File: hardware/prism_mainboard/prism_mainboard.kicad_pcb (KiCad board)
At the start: 2 copper layers, 11 parts, among them U1 XC7Z010-1CLG400C

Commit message: Origin Update
origin update
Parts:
- added C10: 10uF, Capacitor_SMD:C_0805_2012Metric, F.Cu at (251.5, 116.3)
- added C11: 4.7uF, Capacitor_SMD:C_0805_2012Metric, F.Cu at (251.5, 119.3)
- added C12: 2.2uF, Capacitor_SMD:C_0201_0603Metric, F.Cu at (259.5, 122.4)
- added C13: 10uF, Capacitor_SMD:C_0805_2012Metric, F.Cu at (251.5, 122.3)
- added C14: 1uF, Capacitor_SMD:C_0201_0603Metric, F.Cu at (259.5, 124.2)
- added C15: 2.2uF, Capacitor_SMD:C_0201_0603Metric, F.Cu at (259.5, 125.9)
- added C8: 22uF, Capacitor_SMD:C_1206_3216Metric, F.Cu at (256.5, 116.5)
- added C9: 22uF, Capacitor_SMD:C_1206_3216Metric, F.Cu at (256.5, 119.8)
- added L1: 0.47uH, Inductor_SMD:L_0805_2012Metric, F.Cu at (256.0, 122.9)
- added L2: 0.47uH, Inductor_SMD:L_0805_2012Metric, F.Cu at (256.0, 125.7)

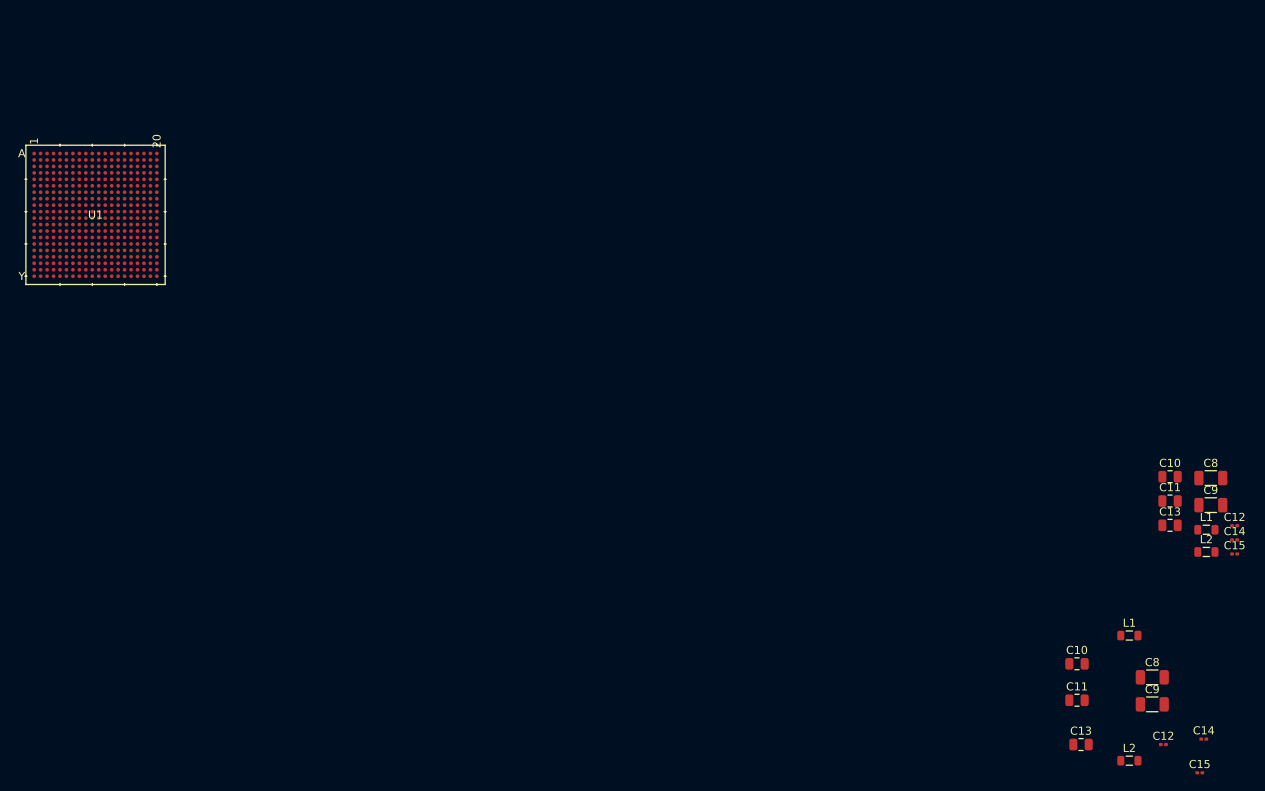
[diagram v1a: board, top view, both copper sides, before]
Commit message: Mainboard Updates
Started a lot of the basic schematic nets like GND and Power nets. Major Change: Decided on using the XC7Z015-1CLG485I instead of the 7010 or 7020 due to the ability to use HDMI interfaces with an adapter and more LUTs. Updated schematic symbols and footprints accordingly. Added Memory, Encoder, MicroSD schematics. Added LimeSDR footprints as well. Will Try to add Power to the entire board next.
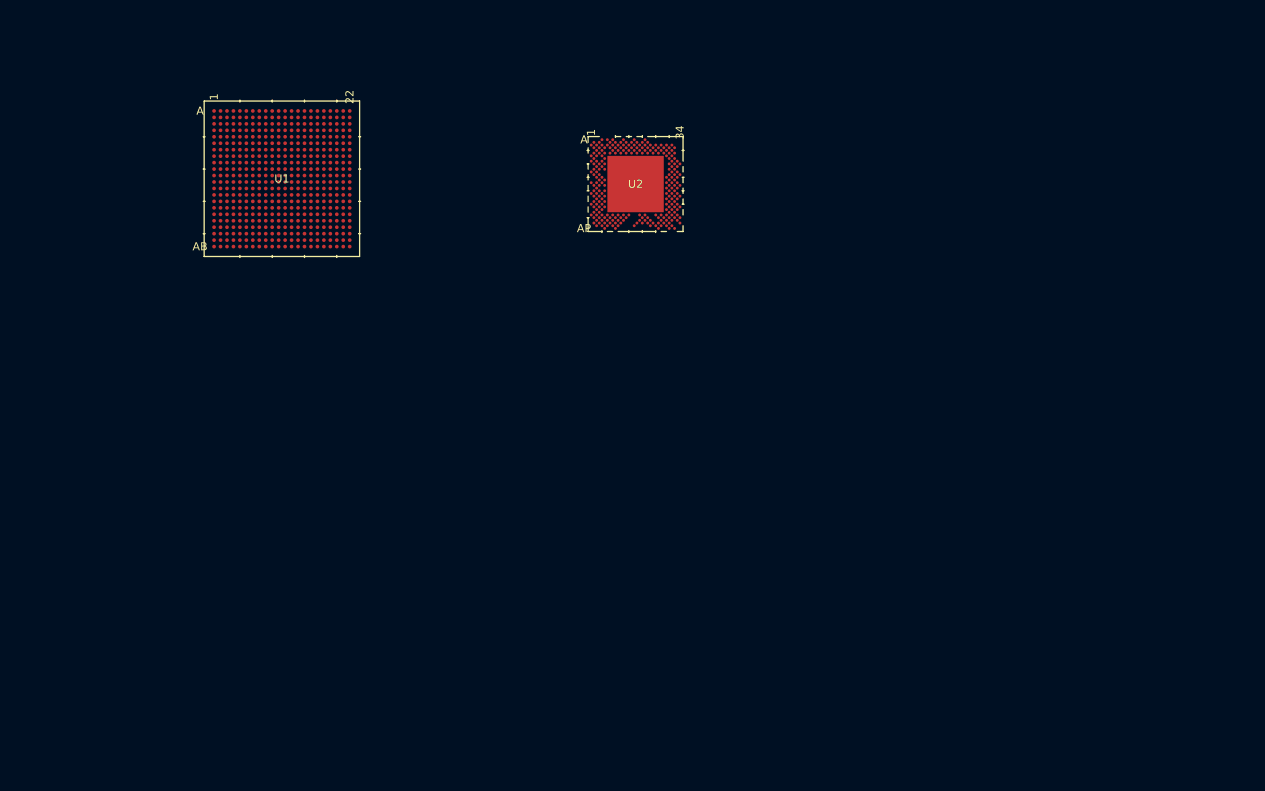
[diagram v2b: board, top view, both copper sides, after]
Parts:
- removed C10 (x2), C13 (x2): 10uF, Capacitor_SMD:C_0805_2012Metric
- removed C11 (x2): 4.7uF, Capacitor_SMD:C_0805_2012Metric
- removed C12 (x2), C15 (x2): 2.2uF, Capacitor_SMD:C_0201_0603Metric
- removed C14 (x2): 1uF, Capacitor_SMD:C_0201_0603Metric
- removed C8 (x2), C9 (x2): 22uF, Capacitor_SMD:C_1206_3216Metric
- removed L1 (x2), L2 (x2): 0.47uH, Inductor_SMD:L_0805_2012Metric
- added U2: LMS7002M, LMS7002M:AQFN261_11P5X11P5_LIM, F.Cu at (185.3, 80.1)
- U1: value XC7Z010-1CLG400C -> XC7Z015-2CLG485I; footprint XC7Z010-1CLG400C:CLG400_XIL -> footprints:CLG485_XIL
- moved U1 23.5 mm to (141.5, 79.4)
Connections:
- U1 pad A10: (no net) -> unconnected-(U1B-PS_MIO26_501-PadA10)
- U1 pad A11: (no net) -> unconnected-(U1B-PS_MIO28_501-PadA11)
- U1 pad A12: (no net) -> unconnected-(U1B-PS_MIO30_501-PadA12)
- U1 pad A13: (no net) -> unconnected-(U1B-VCCO_MIO1_501-PadA13)
- U1 pad A14: (no net) -> unconnected-(U1B-PS_MIO36_501-PadA14)
- U1 pad A15: (no net) -> unconnected-(U1B-PS_MIO20_501-PadA15)
- U1 pad A16: (no net) -> unconnected-(U1B-PS_MIO18_501-PadA16)
- U1 pad A17: (no net) -> unconnected-(U1B-PS_MIO13_500-PadA17)
- U1 pad A18: (no net) -> GND
- U1 pad A19: (no net) -> unconnected-(U1B-PS_MIO6_500-PadA19)
- U1 pad A20: (no net) -> unconnected-(U1B-PS_MIO5_500-PadA20)
- U1 pad A8: unconnected-(U1A-GND-PadA8) -> GND
- U1 pad B10: (no net) -> unconnected-(U1C-VCCO_MIO1_501-PadB10)
- U1 pad B11: (no net) -> unconnected-(U1C-PS_MIO34_501-PadB11)
- U1 pad B12: (no net) -> unconnected-(U1C-PS_MIO43_501-PadB12)
- U1 pad B13: (no net) -> unconnected-(U1C-PS_MIO47_501-PadB13)
- U1 pad B14: (no net) -> unconnected-(U1C-PS_MIO45_501-PadB14)
- U1 pad B15: (no net) -> GND
- U1 pad B16: (no net) -> unconnected-(U1C-PS_MIO24_501-PadB16)
- U1 pad B17: (no net) -> unconnected-(U1C-PS_MIO14_500-PadB17)
- U1 pad B18: (no net) -> unconnected-(U1C-PS_POR_B_500-PadB18)
- U1 pad B19: (no net) -> unconnected-(U1C-PS_MIO11_500-PadB19)
- U1 pad B20: (no net) -> unconnected-(U1C-VCCO_MIO0_500-PadB20)
- U1 pad B5: unconnected-(U1A-PS_MIO9_500-PadB5) -> GND
- U1 pad C10: (no net) -> unconnected-(U1C-PS_MIO39_501-PadC10)
- U1 pad C11: (no net) -> unconnected-(U1C-PS_MIO53_501-PadC11)
- U1 pad C12: (no net) -> GND
- U1 pad C13: (no net) -> unconnected-(U1C-PS_MIO51_501-PadC13)
- U1 pad C14: (no net) -> unconnected-(U1C-PS_SRST_B_501-PadC14)
- U1 pad C15: (no net) -> unconnected-(U1C-PS_MIO41_501-PadC15)
- U1 pad C16: (no net) -> unconnected-(U1C-PS_MIO32_501-PadC16)
- U1 pad C17: (no net) -> unconnected-(U1C-VCCO_MIO0_500-PadC17)
- U1 pad C18: (no net) -> unconnected-(U1C-PS_MIO12_500-PadC18)
- U1 pad C19: (no net) -> unconnected-(U1C-PS_MIO9_500-PadC19)
- U1 pad C2: unconnected-(U1A-PS_DDR_DQS_P0_502-PadC2) -> GND
- U1 pad C20: (no net) -> unconnected-(U1C-PS_DDR_DQ1_502-PadC20)
- U1 pad D10: (no net) -> unconnected-(U1C-PS_MIO50_501-PadD10)
- U1 pad D11: (no net) -> unconnected-(U1C-PS_MIO46_501-PadD11)
- U1 pad D12: (no net) -> unconnected-(U1C-PS_MIO48_501-PadD12)
- U1 pad D13: (no net) -> unconnected-(U1C-PS_MIO52_501-PadD13)
- U1 pad D14: (no net) -> unconnected-(U1C-VCCO_MIO1_501-PadD14)
- U1 pad D15: (no net) -> unconnected-(U1C-PS_MIO42_501-PadD15)
- U1 pad D16: (no net) -> unconnected-(U1C-PS_MIO27_501-PadD16)
- U1 pad D17: (no net) -> unconnected-(U1C-PS_MIO16_501-PadD17)
- U1 pad D18: (no net) -> unconnected-(U1C-PS_MIO7_500-PadD18)
- U1 pad D19: (no net) -> GND
- U1 pad D20: (no net) -> unconnected-(U1C-PS_DDR_DQ3_502-PadD20)
- U1 pad D9: unconnected-(U1A-PS_MIO12_500-PadD9) -> GND
- U1 pad E10: (no net) -> unconnected-(U1C-PS_MIO44_501-PadE10)
- U1 pad E11: (no net) -> unconnected-(U1C-VCCO_MIO1_501-PadE11)
- U1 pad E12: (no net) -> unconnected-(U1C-PS_MIO23_501-PadE12)
- U1 pad E13: (no net) -> unconnected-(U1C-PS_MIO19_501-PadE13)
- U1 pad E14: (no net) -> unconnected-(U1C-PS_MIO17_501-PadE14)
- U1 pad E15: (no net) -> unconnected-(U1C-PS_MIO29_501-PadE15)
- U1 pad E16: (no net) -> GND
- U1 pad E17: (no net) -> unconnected-(U1C-PS_MIO15_500-PadE17)
- U1 pad E18: (no net) -> unconnected-(U1C-PS_MIO8_500-PadE18)
- U1 pad E19: (no net) -> unconnected-(U1C-PS_MIO4_500-PadE19)
- U1 pad E20: (no net) -> unconnected-(U1C-PS_DDR_DQ4_502-PadE20)
- U1 pad E6: unconnected-(U1A-PS_MIO0_500-PadE6) -> GND
- U1 pad F10: (no net) -> unconnected-(U1C-PS_MIO38_501-PadF10)
- U1 pad F11: (no net) -> unconnected-(U1C-PS_MIO25_501-PadF11)
- U1 pad F12: (no net) -> unconnected-(U1C-PS_MIO21_501-PadF12)
- U1 pad F13: (no net) -> GND
- U1 pad F14: (no net) -> unconnected-(U1C-PS_MIO31_501-PadF14)
- U1 pad F15: (no net) -> unconnected-(U1C-PS_MIO_VREF_501-PadF15)
- U1 pad F16: (no net) -> unconnected-(U1C-PS_CLK_500-PadF16)
- U1 pad F17: (no net) -> unconnected-(U1C-PS_MIO3_500-PadF17)
- U1 pad F18: (no net) -> unconnected-(U1C-VCCO_DDR_502-PadF18)
- U1 pad F19: (no net) -> unconnected-(U1C-PS_DDR_A13_502-PadF19)
- U1 pad F20: (no net) -> unconnected-(U1C-PS_DDR_DRST_B_502-PadF20)
- U1 pad F3: unconnected-(U1A-GND-PadF3) -> GND
- U1 pad G10: (no net) -> GND
- U1 pad G11: (no net) -> unconnected-(U1C-PS_MIO33_501-PadG11)
- U1 pad G12: (no net) -> unconnected-(U1C-RSVDGND-PadG12)
- U1 pad G13: (no net) -> VCCPINT
- U1 pad G14: (no net) -> unconnected-(U1C-VCCBATT_0-PadG14)
- U1 pad G15: (no net) -> VCCPINT
- U1 pad G16: (no net) -> unconnected-(U1C-PS_MIO10_500-PadG16)
- U1 pad G17: (no net) -> unconnected-(U1C-PS_MIO0_500-PadG17)
- U1 pad G18: (no net) -> unconnected-(U1C-PS_DDR_A11_502-PadG18)
- U1 pad G19: (no net) -> unconnected-(U1C-PS_DDR_A14_502-PadG19)
- U1 pad G20: (no net) -> GND
- U1 pad H10: (no net) -> unconnected-(U1C-TMS_0-PadH10)
- U1 pad H11: (no net) -> unconnected-(U1C-TCK_0-PadH11)
- U1 pad H12: (no net) -> unconnected-(U1D-VCCBRAM-PadH12)
- U1 pad H13: (no net) -> GND
- U1 pad H14: (no net) -> VCCPINT
- U1 pad H15: (no net) -> GND
- U1 pad H16: (no net) -> unconnected-(U1D-PS_DDR_VREF0_502-PadH16)
- U1 pad H17: (no net) -> GND
- U1 pad H18: (no net) -> unconnected-(U1D-PS_DDR_A9_502-PadH18)
- U1 pad H19: (no net) -> unconnected-(U1D-PS_DDR_A12_502-PadH19)
- U1 pad H20: (no net) -> unconnected-(U1D-PS_DDR_DM1_502-PadH20)
- U1 pad H7: unconnected-(U1A-GND-PadH7) -> GND
- U1 pad J10: (no net) -> GND
- U1 pad J11: (no net) -> VCCINT
- U1 pad J12: (no net) -> GND
- U1 pad J13: (no net) -> unconnected-(U1D-VCCBRAM-PadJ13)
- U1 pad J14: (no net) -> GND
- U1 pad J15: (no net) -> VCCPINT
- U1 pad J16: (no net) -> unconnected-(U1D-PS_DDR_A6_502-PadJ16)
- U1 pad J17: (no net) -> unconnected-(U1D-PS_DDR_A7_502-PadJ17)
- U1 pad J18: (no net) -> unconnected-(U1D-PS_DDR_A8_502-PadJ18)
- U1 pad J19: (no net) -> unconnected-(U1D-VCCO_DDR_502-PadJ19)
- U1 pad J20: (no net) -> unconnected-(U1D-PS_DDR_A10_502-PadJ20)
- U1 pad J4: unconnected-(U1A-PS_DDR_A9_502-PadJ4) -> GND
- U1 pad J9: unconnected-(U1A-VCCADC_0-PadJ9) -> VCCINT
- U1 pad K1: unconnected-(U1A-PS_DDR_A8_502-PadK1) -> GND
- U1 pad K10: (no net) -> VCCINT
- U1 pad K11: (no net) -> unconnected-(U1D-GNDADC_0-PadK11)
- U1 pad K12: (no net) -> unconnected-(U1D-VCCADC_0-PadK12)
- U1 pad K13: (no net) -> GND
- U1 pad K14: (no net) -> unconnected-(U1D-VCCPAUX-PadK14)
- U1 pad K15: (no net) -> GND
- U1 pad K16: (no net) -> unconnected-(U1D-VCCO_DDR_502-PadK16)
- U1 pad K17: (no net) -> unconnected-(U1D-PS_DDR_A4_502-PadK17)
- U1 pad K18: (no net) -> unconnected-(U1D-PS_DDR_A5_502-PadK18)
- U1 pad K19: (no net) -> unconnected-(U1D-PS_DDR_A2_502-PadK19)
- U1 pad K20: (no net) -> unconnected-(U1D-PS_DDR_DQ15_502-PadK20)
- U1 pad K9: unconnected-(U1A-VP_0-PadK9) -> GND
- U1 pad L10: (no net) -> GND
- U1 pad L11: (no net) -> unconnected-(U1D-VREFN_0-PadL11)
- U1 pad L12: (no net) -> unconnected-(U1D-VP_0-PadL12)
- U1 pad L13: (no net) -> unconnected-(U1D-VCCPAUX-PadL13)
- U1 pad L14: (no net) -> GND
- U1 pad L15: (no net) -> VCCPINT
- U1 pad L16: (no net) -> unconnected-(U1D-PS_DDR_BA0_502-PadL16)
- U1 pad L17: (no net) -> unconnected-(U1D-PS_DDR_BA1_502-PadL17)
- U1 pad L18: (no net) -> GND
- U1 pad L19: (no net) -> unconnected-(U1D-PS_DDR_A3_502-PadL19)
- U1 pad L20: (no net) -> unconnected-(U1D-PS_DDR_DQ12_502-PadL20)
- U1 pad L8: unconnected-(U1A-GND-PadL8) -> GND
- U1 pad L9: unconnected-(U1A-VREFP_0-PadL9) -> VCCINT
- U1 pad M10: (no net) -> VCCINT
- U1 pad M11: (no net) -> unconnected-(U1D-VN_0-PadM11)
- U1 pad M12: (no net) -> unconnected-(U1D-VREFP_0-PadM12)
- U1 pad M13: (no net) -> GND
- U1 pad M14: (no net) -> unconnected-(U1D-VCCPAUX-PadM14)
- U1 pad M15: (no net) -> GND
- U1 pad M16: (no net) -> unconnected-(U1D-PS_DDR_VRN_502-PadM16)
- U1 pad M17: (no net) -> unconnected-(U1D-PS_DDR_BA2_502-PadM17)
- U1 pad M18: (no net) -> unconnected-(U1D-PS_DDR_A1_502-PadM18)
- U1 pad M19: (no net) -> unconnected-(U1D-PS_DDR_A0_502-PadM19)
- U1 pad M2: (no net) -> unconnected-(U1B-IO_L15P_T2_DQS_34-PadM2)
- U1 pad M20: (no net) -> unconnected-(U1D-VCCO_DDR_502-PadM20)
- U1 pad M3: (no net) -> unconnected-(U1B-IO_L22N_T3_34-PadM3)
- U1 pad M4: (no net) -> unconnected-(U1B-IO_L22P_T3_34-PadM4)
- U1 pad M5: (no net) -> GND
- U1 pad M6: (no net) -> unconnected-(U1B-IO_L4N_T0_34-PadM6)
- U1 pad M7: (no net) -> unconnected-(U1B-IO_L6N_T0_VREF_34-PadM7)
- U1 pad M8: (no net) -> unconnected-(U1B-IO_L6P_T0_34-PadM8)
- U1 pad M9: (no net) -> GND
- U1 pad N1: (no net) -> unconnected-(U1B-IO_L16P_T2_34-PadN1)
- U1 pad N10: (no net) -> GND
- U1 pad N11: (no net) -> unconnected-(U1D-DXN_0-PadN11)
- U1 pad N12: (no net) -> unconnected-(U1D-DXP_0-PadN12)
- U1 pad N13: (no net) -> VCCAUX
- U1 pad N14: (no net) -> GND
- U1 pad N15: (no net) -> VCCPINT
- U1 pad N16: (no net) -> unconnected-(U1D-PS_DDR_VRP_502-PadN16)
- U1 pad N17: (no net) -> unconnected-(U1D-VCCO_DDR_502-PadN17)
- U1 pad N18: (no net) -> unconnected-(U1D-PS_DDR_CKN_502-PadN18)
- U1 pad N19: (no net) -> unconnected-(U1D-PS_DDR_CKP_502-PadN19)
- U1 pad N2: (no net) -> GND
- U1 pad N20: (no net) -> unconnected-(U1D-PS_DDR_DQ18_502-PadN20)
- U1 pad N3: (no net) -> unconnected-(U1B-IO_L21N_T3_DQS_34-PadN3)
- U1 pad N4: (no net) -> unconnected-(U1B-IO_L21P_T3_DQS_34-PadN4)
- U1 pad N5: (no net) -> unconnected-(U1B-IO_L19N_T3_VREF_34-PadN5)
- U1 pad N6: (no net) -> unconnected-(U1B-IO_L19P_T3_34-PadN6)
- U1 pad N7: (no net) -> unconnected-(U1B-VCCO_34-PadN7)
- U1 pad N8: (no net) -> unconnected-(U1B-IO_L5P_T0_34-PadN8)
- U1 pad N9: (no net) -> VCCINT
- U1 pad P1: (no net) -> unconnected-(U1B-IO_L16N_T2_34-PadP1)
- U1 pad P10: (no net) -> VCCINT
- U1 pad P11: (no net) -> GND
- U1 pad P12: (no net) -> VCCAUX
- U1 pad P13: (no net) -> GND
- U1 pad P14: (no net) -> unconnected-(U1D-VCCPAUX-PadP14)
- U1 pad P15: (no net) -> GND
- U1 pad P16: (no net) -> unconnected-(U1D-PS_DDR_VREF1_502-PadP16)
- U1 pad P17: (no net) -> unconnected-(U1D-PS_DDR_CS_B_502-PadP17)
- U1 pad P18: (no net) -> unconnected-(U1D-PS_DDR_ODT_502-PadP18)
- U1 pad P19: (no net) -> GND
- U1 pad P2: (no net) -> unconnected-(U1B-IO_L18N_T2_34-PadP2)
- U1 pad P20: (no net) -> unconnected-(U1D-PS_DDR_CAS_B_502-PadP20)
- U1 pad P3: (no net) -> unconnected-(U1B-IO_L18P_T2_34-PadP3)
- U1 pad P4: (no net) -> unconnected-(U1B-VCCO_34-PadP4)
- U1 pad P5: (no net) -> unconnected-(U1B-IO_L20N_T3_34-PadP5)
- U1 pad P6: (no net) -> unconnected-(U1B-IO_L20P_T3_34-PadP6)
- U1 pad P7: (no net) -> unconnected-(U1B-IO_L24P_T3_34-PadP7)
- U1 pad P8: (no net) -> unconnected-(U1B-IO_L5N_T0_34-PadP8)
- U1 pad P9: (no net) -> GND
- U1 pad R1: (no net) -> unconnected-(U1B-VCCO_34-PadR1)
- U1 pad R10: (no net) -> unconnected-(U1D-GND-PadR10)
- U1 pad R11: (no net) -> unconnected-(U1D-VCCO_0-PadR11)
- U1 pad R12: (no net) -> GND
- U1 pad R13: (no net) -> VCCAUX
- U1 pad R14: (no net) -> GND
- U1 pad R15: (no net) -> VCCPINT
- U1 pad R16: (no net) -> GND
- U1 pad R17: (no net) -> unconnected-(U1D-IO_L19P_T3_13-PadR17)
- U1 pad R18: (no net) -> unconnected-(U1E-PS_DDR_RAS_B_502-PadR18)
- U1 pad R19: (no net) -> unconnected-(U1E-PS_DDR_WE_B_502-PadR19)
- U1 pad R2: (no net) -> unconnected-(U1B-IO_L17N_T2_34-PadR2)
- U1 pad R20: (no net) -> unconnected-(U1E-PS_DDR_DQ20_502-PadR20)
- U1 pad R3: (no net) -> unconnected-(U1B-IO_L17P_T2_34-PadR3)
- U1 pad R4: (no net) -> unconnected-(U1B-IO_L23N_T3_34-PadR4)
- U1 pad R5: (no net) -> unconnected-(U1B-IO_L23P_T3_34-PadR5)
- U1 pad R6: (no net) -> GND
- U1 pad R7: (no net) -> unconnected-(U1B-IO_L24N_T3_34-PadR7)
- U1 pad R8: (no net) -> unconnected-(U1B-IO_25_34-PadR8)
- U1 pad R9: (no net) -> VCCINT
- U1 pad T1: (no net) -> unconnected-(U1B-IO_L13N_T2_MRCC_34-PadT1)
- U1 pad T10: (no net) -> unconnected-(U1E-DONE_0-PadT10)
- U1 pad T11: (no net) -> unconnected-(U1E-RSVDVCC3-PadT11)
- U1 pad T12: (no net) -> VCCAUX
- U1 pad T13: (no net) -> GND
- U1 pad T14: (no net) -> unconnected-(U1E-RSVDVCC2-PadT14)
- U1 pad T15: (no net) -> unconnected-(U1E-RSVDVCC1-PadT15)
- U1 pad T16: (no net) -> unconnected-(U1E-IO_0_13-PadT16)
- U1 pad T17: (no net) -> unconnected-(U1E-IO_L19N_T3_VREF_13-PadT17)
- U1 pad T18: (no net) -> unconnected-(U1E-VCCO_13-PadT18)
- U1 pad T19: (no net) -> unconnected-(U1E-PS_DDR_CKE_502-PadT19)
- U1 pad T2: (no net) -> unconnected-(U1B-IO_L13P_T2_MRCC_34-PadT2)
- U1 pad T20: (no net) -> unconnected-(U1E-PS_DDR_DQ17_502-PadT20)
- U1 pad T3: (no net) -> GND
- U1 pad T4: (no net) -> GND
- U1 pad T5: (no net) -> GND
- U1 pad T6: (no net) -> GND
- U1 pad T7: (no net) -> GND
- U1 pad T8: (no net) -> GND
- U1 pad T9: (no net) -> unconnected-(U1B-CFGBVS_0-PadT9)
- U1 pad U1: (no net) -> unconnected-(U1B-IO_L14N_T2_SRCC_34-PadU1)
- U1 pad U10: (no net) -> GND
- U1 pad U11: (no net) -> unconnected-(U1E-IO_L5P_T0_13-PadU11)
- U1 pad U12: (no net) -> unconnected-(U1E-IO_L5N_T0_13-PadU12)
- U1 pad U13: (no net) -> unconnected-(U1E-IO_L6P_T0_13-PadU13)
- U1 pad U14: (no net) -> unconnected-(U1E-IO_L6N_T0_VREF_13-PadU14)
- U1 pad U15: (no net) -> unconnected-(U1E-VCCO_13-PadU15)
- U1 pad U16: (no net) -> unconnected-(U1E-IO_25_13-PadU16)
- U1 pad U17: (no net) -> unconnected-(U1E-IO_L22P_T3_13-PadU17)
- U1 pad U18: (no net) -> unconnected-(U1E-IO_L22N_T3_13-PadU18)
- U1 pad U19: (no net) -> unconnected-(U1E-IO_L20P_T3_13-PadU19)
- U1 pad U2: (no net) -> unconnected-(U1B-IO_L14P_T2_SRCC_34-PadU2)
- U1 pad U20: (no net) -> GND
- U1 pad U3: (no net) -> GND
- U1 pad U4: (no net) -> unconnected-(U1B-MGTAVCC-PadU4)
- U1 pad U5: (no net) -> unconnected-(U1B-MGTREFCLK1P_112-PadU5)
- U1 pad U6: (no net) -> unconnected-(U1B-MGTAVCC-PadU6)
- U1 pad U7: (no net) -> unconnected-(U1B-MGTRREF_112-PadU7)
- U1 pad U8: (no net) -> unconnected-(U1B-MGTAVCC-PadU8)
- U1 pad U9: (no net) -> unconnected-(U1B-MGTREFCLK0P_112-PadU9)
- U1 pad V1: (no net) -> GND
- U1 pad V10: (no net) -> unconnected-(U1E-PROGRAM_B_0-PadV10)
- U1 pad V11: (no net) -> unconnected-(U1E-IO_L4P_T0_13-PadV11)
- U1 pad V12: (no net) -> unconnected-(U1E-VCCO_13-PadV12)
- U1 pad V13: (no net) -> unconnected-(U1E-IO_L1P_T0_13-PadV13)
- U1 pad V14: (no net) -> unconnected-(U1E-IO_L1N_T0_13-PadV14)
- U1 pad V15: (no net) -> unconnected-(U1E-IO_L2P_T0_13-PadV15)
- U1 pad V16: (no net) -> unconnected-(U1E-IO_L23P_T3_13-PadV16)
- U1 pad V17: (no net) -> GND
- U1 pad V18: (no net) -> unconnected-(U1E-IO_L21P_T3_DQS_13-PadV18)
- U1 pad V19: (no net) -> unconnected-(U1E-IO_L20N_T3_13-PadV19)
- U1 pad V2: (no net) -> GND
- U1 pad V20: (no net) -> unconnected-(U1E-PS_DDR_DQ30_502-PadV20)
- U1 pad V3: (no net) -> GND
- U1 pad V4: (no net) -> GND
- U1 pad V5: (no net) -> unconnected-(U1B-MGTREFCLK1N_112-PadV5)
- U1 pad V6: (no net) -> GND
- U1 pad V7: (no net) -> unconnected-(U1B-NC-PadV7)
- U1 pad V8: (no net) -> GND
- U1 pad V9: (no net) -> unconnected-(U1B-MGTREFCLK0N_112-PadV9)
- U1 pad W1: (no net) -> GND
- U1 pad W10: (no net) -> GND
- U1 pad W11: (no net) -> unconnected-(U1E-IO_L4N_T0_13-PadW11)
- U1 pad W12: (no net) -> unconnected-(U1E-IO_L3P_T0_DQS_13-PadW12)
- U1 pad W13: (no net) -> unconnected-(U1E-IO_L3N_T0_DQS_13-PadW13)
- U1 pad W14: (no net) -> GND
- U1 pad W15: (no net) -> unconnected-(U1E-IO_L2N_T0_13-PadW15)
- U1 pad W16: (no net) -> unconnected-(U1E-IO_L23N_T3_13-PadW16)
- U1 pad W17: (no net) -> unconnected-(U1E-IO_L24P_T3_13-PadW17)
- U1 pad W18: (no net) -> unconnected-(U1E-IO_L21N_T3_DQS_13-PadW18)
- U1 pad W19: (no net) -> unconnected-(U1E-VCCO_13-PadW19)
- U1 pad W2: (no net) -> unconnected-(U1B-MGTPTXP3_112-PadW2)
- U1 pad W20: (no net) -> unconnected-(U1E-PS_DDR_DQ29_502-PadW20)
- U1 pad W3: (no net) -> unconnected-(U1B-NC-PadW3)
- U1 pad W4: (no net) -> unconnected-(U1B-MGTPTXP1_112-PadW4)
- U1 pad W5: (no net) -> unconnected-(U1B-MGTAVCC-PadW5)
- U1 pad W6: (no net) -> unconnected-(U1B-MGTPRXP3_112-PadW6)
- U1 pad W7: (no net) -> GND
- U1 pad W8: (no net) -> unconnected-(U1B-MGTPRXP1_112-PadW8)
- U1 pad W9: (no net) -> unconnected-(U1B-MGTAVCC-PadW9)
- U1 pad Y1: (no net) -> GND
- U1 pad Y10: (no net) -> GND
- U1 pad Y11: (no net) -> GND
- U1 pad Y12: (no net) -> unconnected-(U1E-IO_L10P_T1_13-PadY12)
- U1 pad Y13: (no net) -> unconnected-(U1E-IO_L10N_T1_13-PadY13)
- U1 pad Y14: (no net) -> unconnected-(U1E-IO_L12P_T1_MRCC_13-PadY14)
- U1 pad Y15: (no net) -> unconnected-(U1E-IO_L12N_T1_MRCC_13-PadY15)
- U1 pad Y16: (no net) -> unconnected-(U1E-VCCO_13-PadY16)
- U1 pad Y17: (no net) -> unconnected-(U1E-IO_L24N_T3_13-PadY17)
- U1 pad Y18: (no net) -> unconnected-(U1E-IO_L13P_T2_MRCC_13-PadY18)
- U1 pad Y19: (no net) -> unconnected-(U1E-IO_L13N_T2_MRCC_13-PadY19)
- U1 pad Y2: (no net) -> unconnected-(U1B-MGTPTXN3_112-PadY2)
- U1 pad Y20: (no net) -> unconnected-(U1E-PS_DDR_DQ24_502-PadY20)
- U1 pad Y3: (no net) -> GND
- U1 pad Y4: (no net) -> unconnected-(U1B-MGTPTXN1_112-PadY4)
- U1 pad Y5: (no net) -> GND
- U1 pad Y6: (no net) -> unconnected-(U1B-MGTPRXN3_112-PadY6)
- U1 pad Y7: (no net) -> unconnected-(U1B-MGTAVTT-PadY7)
- U1 pad Y8: (no net) -> unconnected-(U1B-MGTPRXN1_112-PadY8)
- U1 pad Y9: (no net) -> GND
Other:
- copper layers 2 -> 6

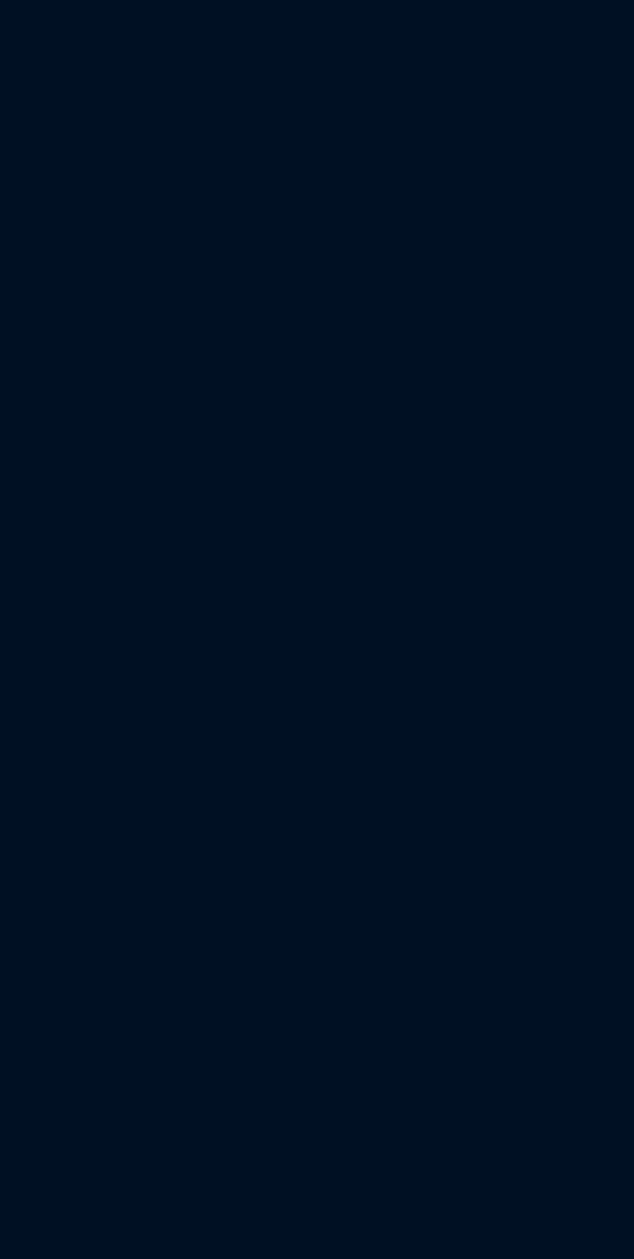
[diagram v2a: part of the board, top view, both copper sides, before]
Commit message: Schematic Updates
Updated schematics. Most of the power and decoupling is set for most if not all devices. Need to interconnect devices. Still reading datasheets
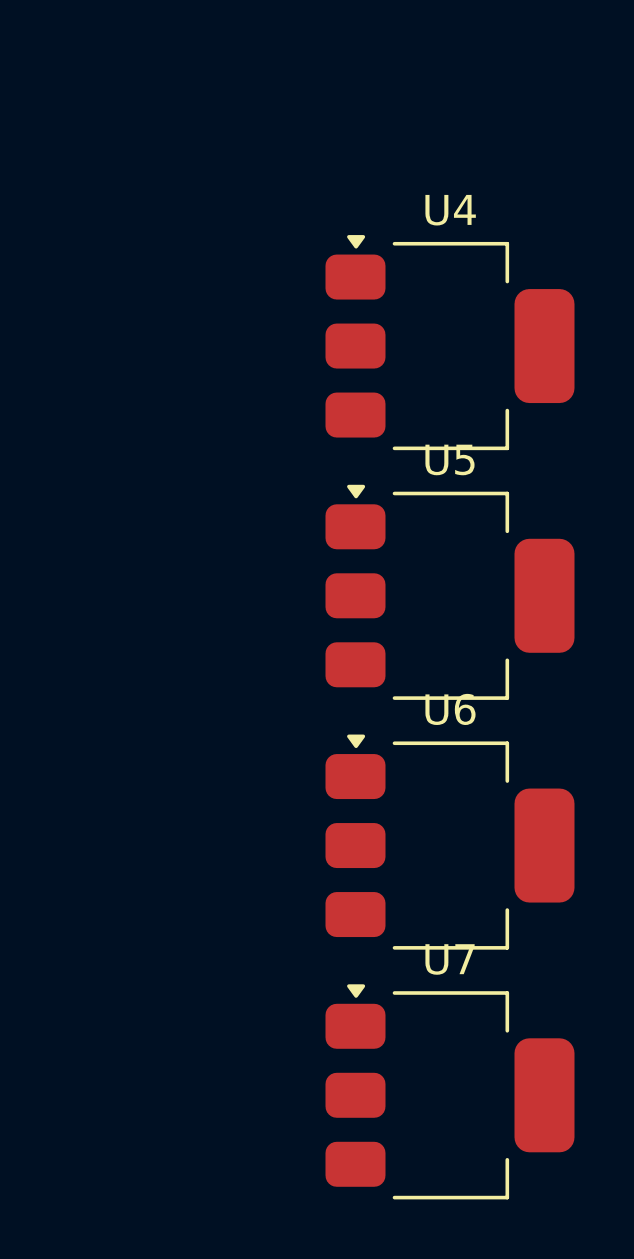
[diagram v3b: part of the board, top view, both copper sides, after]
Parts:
- added U4: AMS1117-1.8, Package_TO_SOT_SMD:SOT-223-3_TabPin2, F.Cu at (232.9, 99.2)
- added U5: AMS1117-1.8, Package_TO_SOT_SMD:SOT-223-3_TabPin2, F.Cu at (232.9, 107.5)
- added U6: AMS1117-1.8, Package_TO_SOT_SMD:SOT-223-3_TabPin2, F.Cu at (232.9, 115.8)
- added U7: AMS1117-1.8, Package_TO_SOT_SMD:SOT-223-3_TabPin2, F.Cu at (232.9, 124.2)
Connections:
- U1 pad A13: unconnected-(U1B-VCCO_MIO1_501-PadA13) -> VCCO_0
- U1 pad A3: unconnected-(U1A-VCCO_35-PadA3) -> VCCAUX
- U1 pad B10: unconnected-(U1C-VCCO_MIO1_501-PadB10) -> VCCO_0
- U1 pad B20: unconnected-(U1C-VCCO_MIO0_500-PadB20) -> VCCAUX
- U1 pad C17: unconnected-(U1C-VCCO_MIO0_500-PadC17) -> VCCAUX
- U1 pad C7: unconnected-(U1A-VCCO_35-PadC7) -> VCCAUX
- U1 pad D14: unconnected-(U1C-VCCO_MIO1_501-PadD14) -> VCCO_0
- U1 pad D18: unconnected-(U1C-PS_MIO7_500-PadD18) -> Net-(U1C-PS_MIO7_500)
- U1 pad D4: unconnected-(U1A-VCCO_35-PadD4) -> VCCAUX
- U1 pad E1: unconnected-(U1A-VCCO_35-PadE1) -> VCCAUX
- U1 pad E11: unconnected-(U1C-VCCO_MIO1_501-PadE11) -> VCCO_0
- U1 pad E18: unconnected-(U1C-PS_MIO8_500-PadE18) -> Net-(U1C-PS_MIO8_500)
- U1 pad E21: unconnected-(U1C-VCCO_DDR_502-PadE21) -> VCCO_DDR
- U1 pad F18: unconnected-(U1C-VCCO_DDR_502-PadF18) -> VCCO_DDR
- U1 pad F8: unconnected-(U1A-VCCO_35-PadF8) -> VCCAUX
- U1 pad G13: VCCPINT -> VCCINT
- U1 pad G15: VCCPINT -> VCCINT
- U1 pad G5: unconnected-(U1A-VCCO_35-PadG5) -> VCCAUX
- U1 pad H12: unconnected-(U1D-VCCBRAM-PadH12) -> VCCBRAM
- U1 pad H14: VCCPINT -> VCCINT
- U1 pad H2: unconnected-(U1A-VCCO_34-PadH2) -> VCCAUX
- U1 pad H22: unconnected-(U1D-VCCO_DDR_502-PadH22) -> VCCO_DDR
- U1 pad J13: unconnected-(U1D-VCCBRAM-PadJ13) -> VCCBRAM
- U1 pad J15: VCCPINT -> VCCINT
- U1 pad J19: unconnected-(U1D-VCCO_DDR_502-PadJ19) -> VCCO_DDR
- U1 pad K11: unconnected-(U1D-GNDADC_0-PadK11) -> GND
- U1 pad K14: unconnected-(U1D-VCCPAUX-PadK14) -> VCCAUX
- U1 pad K16: unconnected-(U1D-VCCO_DDR_502-PadK16) -> VCCO_DDR
- U1 pad K6: unconnected-(U1A-VCCO_34-PadK6) -> VCCAUX
- U1 pad L13: unconnected-(U1D-VCCPAUX-PadL13) -> VCCAUX
- U1 pad L15: VCCPINT -> VCCINT
- U1 pad L3: unconnected-(U1A-VCCO_34-PadL3) -> VCCAUX
- U1 pad M14: unconnected-(U1D-VCCPAUX-PadM14) -> VCCAUX
- U1 pad M20: unconnected-(U1D-VCCO_DDR_502-PadM20) -> VCCO_DDR
- U1 pad N15: VCCPINT -> VCCINT
- U1 pad N17: unconnected-(U1D-VCCO_DDR_502-PadN17) -> VCCO_DDR
- U1 pad N7: unconnected-(U1B-VCCO_34-PadN7) -> VCCAUX
- U1 pad P14: unconnected-(U1D-VCCPAUX-PadP14) -> VCCAUX
- U1 pad P4: unconnected-(U1B-VCCO_34-PadP4) -> VCCAUX
- U1 pad R1: unconnected-(U1B-VCCO_34-PadR1) -> VCCAUX
- U1 pad R11: unconnected-(U1D-VCCO_0-PadR11) -> VCCO_0
- U1 pad R15: VCCPINT -> VCCINT
- U1 pad R21: unconnected-(U1E-VCCO_DDR_502-PadR21) -> VCCO_DDR
- U1 pad V22: unconnected-(U1E-VCCO_DDR_502-PadV22) -> VCCO_DDR
- U2 pad AE3: unconnected-(U2A-VDD18_TIA_RFE-PadAE3) -> VDD_1V8
- U2 pad AF4: unconnected-(U2A-VDD18_LDO_RX-PadAF4) -> VDD_1V8_LDO
- U2 pad AH30: unconnected-(U2C-DIGPRVDD2-PadAH30) -> VDD_1V8_DIG
- U2 pad AK22: unconnected-(U2C-VDD18_VCO_SXR-PadAK22) -> VDD_1V8
- U2 pad AM18: unconnected-(U2C-VDD18_SXR-PadAM18) -> VDD_1V8
- U2 pad AM26: unconnected-(U2C-VDD18_RXBUF-PadAM26) -> VDD_1V8
- U2 pad D16: unconnected-(U2B-VDD18_TRF-PadD16) -> VDD_1V8
- U2 pad D24: unconnected-(U2B-VDD18_DIG-PadD24) -> VDD_1V8
- U2 pad E17: unconnected-(U2B-VDD18_BIAS-PadE17) -> VDD_1V8
- U2 pad E21: unconnected-(U2B-VDD18_VCO_CGEN-PadE21) -> VDD_1V8
- U2 pad G3: unconnected-(U2A-VDD18_VCO_SXT-PadG3) -> VDD_1V8
- U2 pad H32: unconnected-(U2B-DIGPRVDD2-PadH32) -> VDD_1V8_DIG
- U2 pad N1: unconnected-(U2A-VDD18_LDO_TX-PadN1) -> VDD_1V8_LDO
- U2 pad T32: unconnected-(U2C-DIGPRVDD2/DIGPRPOC-PadT32) -> VDD_1V8_DIG
- U2 pad U33: unconnected-(U2C-CORE_LDO_EN-PadU33) -> NC
